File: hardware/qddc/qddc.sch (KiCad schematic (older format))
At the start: 37 parts, among them IC1 FST3253MTCX, IC2 OPA2350UA, J1 In_cos, J2 In_sin, J3 In_RF, J4 PWR, J5 Out_I, J6 Out_Q, T1 ETC4-1-2TR

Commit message: Start PCB for Quad DDC
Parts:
- C1, C10, C11, C12, C13, C2, C3, C4, C5, C6, C7, C8, C9: footprint (none) -> Capacitor_SMD:C_0805_2012Metric
- IC1: footprint SOP65P640X110-16N -> FST3253MTCX:SOP65P640X110-16N
- IC2: footprint SOIC127P600X175-8N -> OPA2350UA:SOIC127P600X175-8N
- J1, J2, J3, J5, J6: footprint (none) -> Connector_Coaxial:SMA_Amphenol_132289_EdgeMount
- J4: footprint (none) -> Connector_PinHeader_2.54mm:PinHeader_1x04_P2.54mm_Vertical
- L1: footprint (none) -> Inductor_SMD:L_1206_3216Metric
- R1, R10, R11, R12, R13, R14, R2, R3, R4, R5, R6, R7, R8, R9: footprint (none) -> Resistor_SMD:R_0805_2012Metric
- T1: footprint E_SERIES_1 -> ETC4-1-2TR:E_SERIES_1
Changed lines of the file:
@@
 F 0 "IC1" H 4550 2915 50  0000 C CNN
 F 1 "FST3253MTCX" H 4550 2824 50  0000 C CNN
-F 2 "SOP65P640X110-16N" H 4950 2750 50  0001 L CNN
+F 2 "FST3253MTCX:SOP65P640X110-16N" H 4950 2750 50  0001 L CNN
 F 3 "https://componentsearchengine.com/Datasheets/2/FST3253MTCX.pdf" H 4950 2650 50  0001 L CNN
 F 4 "IC, Fairchild, FST3253MTCX Fairchild Semiconductor FST3253MTCX, Multiplexer/Demultiplexer Dual 4:1 Multiplexer, 4  5.5 V, 16-Pin TSSOP" H 4950 2550 50  0001 L CNN "Description"
@@
 F 0 "T1" H 2625 3575 50  0000 C CNN
 F 1 "ETC4-1-2TR" H 2625 3484 50  0000 C CNN
-F 2 "E_SERIES_1" H 3400 3400 50  0001 L CNN
+F 2 "ETC4-1-2TR:E_SERIES_1" H 3400 3400 50  0001 L CNN
 F 3 "https://cdn.macom.com/datasheets/ETC4-1-2-TR.pdf" H 3400 3300 50  0001 L CNN
 F 4 "Audio Transformers / Signal Transformers 2-800MHz Imp. Ratio 1:4" H 3400 3200 50  0001 L CNN "Description"
@@
 F 0 "J3" H 1950 3532 50  0000 L CNN
 F 1 "In_RF" H 1950 3623 50  0000 L CNN
-F 2 "" H 1850 3650 50  0001 C CNN
+F 2 "Connector_Coaxial:SMA_Amphenol_132289_EdgeMount" H 1850 3650 50  0001 C CNN
 F 3 " ~" H 1850 3650 50  0001 C CNN
 	1    1850 3650
@@
 F 0 "R3" V 3093 3250 50  0000 C CNN
 F 1 "47" V 3184 3250 50  0000 C CNN
-F 2 "" V 3230 3250 50  0001 C CNN
+F 2 "Resistor_SMD:R_0805_2012Metric" V 3230 3250 50  0001 C CNN
 F 3 "~" H 3300 3250 50  0001 C CNN
 	1    3300 3250
@@
 F 0 "R4" V 3093 3650 50  0000 C CNN
 F 1 "47" V 3184 3650 50  0000 C CNN
-F 2 "" V 3230 3650 50  0001 C CNN
+F 2 "Resistor_SMD:R_0805_2012Metric" V 3230 3650 50  0001 C CNN
 F 3 "~" H 3300 3650 50  0001 C CNN
 	1    3300 3650
@@
 F 0 "R7" V 6243 2950 50  0000 C CNN
 F 1 "100" V 6334 2950 50  0000 C CNN
-F 2 "" V 6380 2950 50  0001 C CNN
+F 2 "Resistor_SMD:R_0805_2012Metric" V 6380 2950 50  0001 C CNN
 F 3 "~" H 6450 2950 50  0001 C CNN
 	1    6450 2950
@@
 F 0 "R8" V 6243 3250 50  0000 C CNN
 F 1 "100" V 6334 3250 50  0000 C CNN
-F 2 "" V 6380 3250 50  0001 C CNN
+F 2 "Resistor_SMD:R_0805_2012Metric" V 6380 3250 50  0001 C CNN
 F 3 "~" H 6450 3250 50  0001 C CNN
 	1    6450 3250
@@
 F 0 "R9" V 6243 3650 50  0000 C CNN
 F 1 "100" V 6334 3650 50  0000 C CNN
-F 2 "" V 6380 3650 50  0001 C CNN
+F 2 "Resistor_SMD:R_0805_2012Metric" V 6380 3650 50  0001 C CNN
 F 3 "~" H 6450 3650 50  0001 C CNN
 	1    6450 3650
@@
 F 0 "R10" V 6243 3950 50  0000 C CNN
 F 1 "100" V 6334 3950 50  0000 C CNN
-F 2 "" V 6380 3950 50  0001 C CNN
+F 2 "Resistor_SMD:R_0805_2012Metric" V 6380 3950 50  0001 C CNN
 F 3 "~" H 6450 3950 50  0001 C CNN
 	1    6450 3950
@@
 F 0 "C7" H 6315 2446 50  0000 L CNN
 F 1 "22nF" H 6315 2355 50  0000 L CNN
-F 2 "" H 6238 2250 50  0001 C CNN
+F 2 "Capacitor_SMD:C_0805_2012Metric" H 6238 2250 50  0001 C CNN
 F 3 "~" H 6200 2400 50  0001 C CNN
 	1    6200 2400
@@
 F 0 "C5" H 5915 2446 50  0000 L CNN
 F 1 "22nF" H 5915 2355 50  0000 L CNN
-F 2 "" H 5838 2250 50  0001 C CNN
+F 2 "Capacitor_SMD:C_0805_2012Metric" H 5838 2250 50  0001 C CNN
 F 3 "~" H 5800 2400 50  0001 C CNN
 	1    5800 2400
@@
 F 0 "C8" H 6315 4346 50  0000 L CNN
 F 1 "22nF" H 6315 4255 50  0000 L CNN
-F 2 "" H 6238 4150 50  0001 C CNN
+F 2 "Capacitor_SMD:C_0805_2012Metric" H 6238 4150 50  0001 C CNN
 F 3 "~" H 6200 4300 50  0001 C CNN
 	1    6200 4300
@@
 F 0 "C6" H 5915 4346 50  0000 L CNN
 F 1 "22nF" H 5915 4255 50  0000 L CNN
-F 2 "" H 5838 4150 50  0001 C CNN
+F 2 "Capacitor_SMD:C_0805_2012Metric" H 5838 4150 50  0001 C CNN
 F 3 "~" H 5800 4300 50  0001 C CNN
 	1    5800 4300
@@
 F 0 "J2" H 1949 2632 50  0000 L CNN
 F 1 "In_sin" H 1949 2723 50  0000 L CNN
-F 2 "" H 1850 2750 50  0001 C CNN
+F 2 "Connector_Coaxial:SMA_Amphenol_132289_EdgeMount" H 1850 2750 50  0001 C CNN
 F 3 " ~" H 1850 2750 50  0001 C CNN
 	1    1850 2750
@@
 F 0 "C9" H 6665 2446 50  0000 L CNN
 F 1 "390" H 6665 2355 50  0000 L CNN
-F 2 "" H 6588 2250 50  0001 C CNN
+F 2 "Capacitor_SMD:C_0805_2012Metric" H 6588 2250 50  0001 C CNN
 F 3 "~" H 6550 2400 50  0001 C CNN
 	1    6550 2400
@@
 F 0 "R11" H 6970 2446 50  0000 L CNN
 F 1 "2.2k" H 6970 2355 50  0000 L CNN
-F 2 "" V 6830 2400 50  0001 C CNN
+F 2 "Resistor_SMD:R_0805_2012Metric" V 6830 2400 50  0001 C CNN
 F 3 "~" H 6900 2400 50  0001 C CNN
 	1    6900 2400
@@
 F 0 "R12" V 7293 2150 50  0000 C CNN
 F 1 "100" V 7384 2150 50  0000 C CNN
-F 2 "" V 7430 2150 50  0001 C CNN
+F 2 "Resistor_SMD:R_0805_2012Metric" V 7430 2150 50  0001 C CNN
 F 3 "~" H 7500 2150 50  0001 C CNN
 	1    7500 2150
@@
 F 0 "R13" H 8870 2996 50  0000 L CNN
 F 1 "100" H 8870 2905 50  0000 L CNN
-F 2 "" V 8730 2950 50  0001 C CNN
+F 2 "Resistor_SMD:R_0805_2012Metric" V 8730 2950 50  0001 C CNN
 F 3 "~" H 8800 2950 50  0001 C CNN
 	1    8800 2950
@@
 F 0 "J6" H 9600 2675 50  0000 L CNN
 F 1 "Out_Q" H 9600 2584 50  0000 L CNN
-F 2 "" H 9500 2700 50  0001 C CNN
+F 2 "Connector_Coaxial:SMA_Amphenol_132289_EdgeMount" H 9500 2700 50  0001 C CNN
 F 3 " ~" H 9500 2700 50  0001 C CNN
 	1    9500 2700
@@
 F 0 "J5" H 9600 2125 50  0000 L CNN
 F 1 "Out_I" H 9600 2034 50  0000 L CNN
-F 2 "" H 9500 2150 50  0001 C CNN
+F 2 "Connector_Coaxial:SMA_Amphenol_132289_EdgeMount" H 9500 2150 50  0001 C CNN
 F 3 " ~" H 9500 2150 50  0001 C CNN
 	1    9500 2150
@@
 F 0 "R2" V 3093 2750 50  0000 C CNN
 F 1 "100" V 3184 2750 50  0000 C CNN
-F 2 "" V 3230 2750 50  0001 C CNN
+F 2 "Resistor_SMD:R_0805_2012Metric" V 3230 2750 50  0001 C CNN
 F 3 "~" H 3300 2750 50  0001 C CNN
 	1    3300 2750
@@
 F 0 "R1" V 3093 2150 50  0000 C CNN
 F 1 "100" V 3184 2150 50  0000 C CNN
-F 2 "" V 3230 2150 50  0001 C CNN
+F 2 "Resistor_SMD:R_0805_2012Metric" V 3230 2150 50  0001 C CNN
 F 3 "~" H 3300 2150 50  0001 C CNN
 	1    3300 2150
@@
 F 0 "R5" H 4020 4996 50  0000 L CNN
 F 1 "1k" H 4020 4905 50  0000 L CNN
-F 2 "" V 3880 4950 50  0001 C CNN
+F 2 "Resistor_SMD:R_0805_2012Metric" V 3880 4950 50  0001 C CNN
 F 3 "~" H 3950 4950 50  0001 C CNN
 	1    3950 4950
@@
 F 0 "R6" H 4020 5396 50  0000 L CNN
 F 1 "1k" H 4020 5305 50  0000 L CNN
-F 2 "" V 3880 5350 50  0001 C CNN
+F 2 "Resistor_SMD:R_0805_2012Metric" V 3880 5350 50  0001 C CNN
 F 3 "~" H 3950 5350 50  0001 C CNN
 	1    3950 5350
@@
 F 0 "C3" H 4465 5196 50  0000 L CNN
 F 1 "100nF" H 4465 5105 50  0000 L CNN
-F 2 "" H 4388 5000 50  0001 C CNN
+F 2 "Capacitor_SMD:C_0805_2012Metric" H 4388 5000 50  0001 C CNN
 F 3 "~" H 4350 5150 50  0001 C CNN
 	1    4350 5150
@@
 F 0 "C1" H 3115 5396 50  0000 L CNN
 F 1 "100nF" H 3115 5305 50  0000 L CNN
-F 2 "" H 3038 5200 50  0001 C CNN
+F 2 "Capacitor_SMD:C_0805_2012Metric" H 3038 5200 50  0001 C CNN
 F 3 "~" H 3000 5350 50  0001 C CNN
 	1    3000 5350
@@
 F 0 "C2" H 3618 5396 50  0000 L CNN
 F 1 "10nF" H 3618 5305 50  0000 L CNN
-F 2 "" H 3538 5200 50  0001 C CNN
+F 2 "Capacitor_SMD:C_0805_2012Metric" H 3538 5200 50  0001 C CNN
 F 3 "~" H 3500 5350 50  0001 C CNN
 	1    3500 5350
@@
 F 0 "L1" V 4840 4700 50  0000 C CNN
 F 1 "47uH" V 4749 4700 50  0000 C CNN
-F 2 "" H 4650 4700 50  0001 C CNN
+F 2 "Inductor_SMD:L_1206_3216Metric" H 4650 4700 50  0001 C CNN
 F 3 "~" H 4650 4700 50  0001 C CNN
 	1    4650 4700
@@
 F 0 "C4" H 5265 2446 50  0000 L CNN
 F 1 "100nF" H 5265 2355 50  0000 L CNN
-F 2 "" H 5188 2250 50  0001 C CNN
+F 2 "Capacitor_SMD:C_0805_2012Metric" H 5188 2250 50  0001 C CNN
 F 3 "~" H 5150 2400 50  0001 C CNN
 	1    5150 2400
@@
 F 0 "J1" H 1950 2032 50  0000 L CNN
 F 1 "In_cos" H 1950 2123 50  0000 L CNN
-F 2 "" H 1850 2150 50  0001 C CNN
+F 2 "Connector_Coaxial:SMA_Amphenol_132289_EdgeMount" H 1850 2150 50  0001 C CNN
 F 3 " ~" H 1850 2150 50  0001 C CNN
 	1    1850 2150
@@
 F 0 "C10" H 9315 3646 50  0000 L CNN
 F 1 "390" H 9315 3555 50  0000 L CNN
-F 2 "" H 9238 3450 50  0001 C CNN
+F 2 "Capacitor_SMD:C_0805_2012Metric" H 9238 3450 50  0001 C CNN
 F 3 "~" H 9200 3600 50  0001 C CNN
 	1    9200 3600
@@
 F 0 "IC2" H 7750 3415 50  0000 C CNN
 F 1 "OPA2350UA" H 7750 3324 50  0000 C CNN
-F 2 "SOIC127P600X175-8N" H 8200 3250 50  0001 L CNN
+F 2 "OPA2350UA:SOIC127P600X175-8N" H 8200 3250 50  0001 L CNN
 F 3 "http://www.ti.com/lit/ds/symlink/opa2350.pdf" H 8200 3150 50  0001 L CNN
 F 4 "High-Speed, Single-Supply, Rail-to-Rail Operational Amplifiers MicroAmplifier Series" H 8200 3050 50  0001 L CNN "Description"
@@
 F 0 "R14" H 8870 3646 50  0000 L CNN
 F 1 "2.2k" H 8870 3555 50  0000 L CNN
-F 2 "" V 8730 3600 50  0001 C CNN
+F 2 "Resistor_SMD:R_0805_2012Metric" V 8730 3600 50  0001 C CNN
 F 3 "~" H 8800 3600 50  0001 C CNN
 	1    8800 3600
@@
 F 0 "J4" H 8072 4624 50  0000 R CNN
 F 1 "PWR" H 8072 4533 50  0000 R CNN
-F 2 "" H 8100 4650 50  0001 C CNN
+F 2 "Connector_PinHeader_2.54mm:PinHeader_1x04_P2.54mm_Vertical" H 8100 4650 50  0001 C CNN
 F 3 "~" H 8100 4650 50  0001 C CNN
 	1    8100 4650
@@
 F 0 "C11" H 8465 2896 50  0000 L CNN
 F 1 "100nF" H 8465 2805 50  0000 L CNN
-F 2 "" H 8388 2700 50  0001 C CNN
+F 2 "Capacitor_SMD:C_0805_2012Metric" H 8388 2700 50  0001 C CNN
 F 3 "~" H 8350 2850 50  0001 C CNN
 	1    8350 2850
@@
 F 0 "C12" V 8798 2150 50  0000 C CNN
 F 1 "470nF" V 8889 2150 50  0000 C CNN
-F 2 "" H 9088 2000 50  0001 C CNN
+F 2 "Capacitor_SMD:C_0805_2012Metric" H 9088 2000 50  0001 C CNN
 F 3 "~" H 9050 2150 50  0001 C CNN
 	1    9050 2150
@@
 F 0 "C13" V 8798 2700 50  0000 C CNN
 F 1 "470nF" V 8889 2700 50  0000 C CNN
-F 2 "" H 9088 2550 50  0001 C CNN
+F 2 "Capacitor_SMD:C_0805_2012Metric" H 9088 2550 50  0001 C CNN
 F 3 "~" H 9050 2700 50  0001 C CNN
 	1    9050 2700
@@
 	5800 2250 5150 2250
 $Comp
-L power:GND #PWR?
+L power:GND #PWR0104
 U 1 1 6023AE13
 P 5800 2100
-F 0 "#PWR?" H 5800 1850 50  0001 C CNN
+F 0 "#PWR0104" H 5800 1850 50  0001 C CNN
 F 1 "GND" H 5805 1927 50  0000 C CNN
 F 2 "" H 5800 2100 50  0001 C CNN

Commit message: PCB for Quad DDC
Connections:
- net GND: now also J4.1 (Pin_1); no longer J4.4 (Pin_4)
- net PTT: now also J4.4 (Pin_4); no longer J4.1 (Pin_1)
- net at IC2.6 (-IN_B), R10.1, R14.2: now also C10.1; no longer C10.2
- net at IC2.7 (OUT_B), R13.2, R14.1: now also C10.2; no longer C10.1
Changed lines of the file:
@@
 L power:GND #PWR0114
 U 1 1 602C6C44
-P 7200 4850
-F 0 "#PWR0114" H 7200 4600 50  0001 C CNN
-F 1 "GND" V 7205 4722 50  0000 R CNN
-F 2 "" H 7200 4850 50  0001 C CNN
-F 3 "" H 7200 4850 50  0001 C CNN
-	1    7200 4850
+P 7200 4550
+F 0 "#PWR0114" H 7200 4300 50  0001 C CNN
+F 1 "GND" V 7205 4422 50  0000 R CNN
+F 2 "" H 7200 4550 50  0001 C CNN
+F 3 "" H 7200 4550 50  0001 C CNN
+	1    7200 4550
 	0    1    1    0
 $EndComp
@@
 $EndComp
 Wire Wire Line
-	7200 4750 7550 4750
-Wire Wire Line
 	3000 3450 3000 5150
 Connection ~ 3000 5150
@@
 U 1 1 601C8840
 P 9200 3600
-F 0 "C10" H 9315 3646 50  0000 L CNN
-F 1 "390" H 9315 3555 50  0000 L CNN
+F 0 "C10" H 8950 3650 50  0000 L CNN
+F 1 "390" H 8950 3550 50  0000 L CNN
 F 2 "Capacitor_SMD:C_0805_2012Metric" H 9238 3450 50  0001 C CNN
 F 3 "~" H 9200 3600 50  0001 C CNN
 	1    9200 3600
-	1    0    0    -1
+	-1   0    0    1
 $EndComp
 $Comp
@@
 U 1 1 601C7CA8
 P 8800 3600
-F 0 "R14" H 8870 3646 50  0000 L CNN
-F 1 "2.2k" H 8870 3555 50  0000 L CNN
+F 0 "R14" H 8850 3650 50  0000 L CNN
+F 1 "2.2k" H 8850 3550 50  0000 L CNN
 F 2 "Resistor_SMD:R_0805_2012Metric" V 8730 3600 50  0001 C CNN
 F 3 "~" H 8800 3600 50  0001 C CNN
@@
 	6900 3250 7150 3250
 Connection ~ 7150 2150
-$Comp
-L power:PWR_FLAG #FLG0101
-U 1 1 60403D64
-P 7550 4950
-F 0 "#FLG0101" H 7550 5025 50  0001 C CNN
-F 1 "PWR_FLAG" H 7550 5123 50  0000 C CNN
-F 2 "" H 7550 4950 50  0001 C CNN
-F 3 "~" H 7550 4950 50  0001 C CNN
-	1    7550 4950
-	-1   0    0    1
-$EndComp
-Wire Wire Line
-	7550 4750 7900 4750
 $Comp
 L power:VAA #PWR0116
@@
 $EndComp
 $Comp
-L power:PWR_FLAG #FLG0102
-U 1 1 6041AEE4
-P 7550 4550
-F 0 "#FLG0102" H 7550 4625 50  0001 C CNN
-F 1 "PWR_FLAG" H 7550 4723 50  0000 C CNN
-F 2 "" H 7550 4550 50  0001 C CNN
-F 3 "~" H 7550 4550 50  0001 C CNN
-	1    7550 4550
-	1    0    0    -1
-$EndComp
-Wire Wire Line
-	7550 4750 7550 4950
-Connection ~ 7550 4750
-Wire Wire Line
-	7200 4850 7300 4850
-Wire Wire Line
-	7200 4650 7550 4650
-Wire Wire Line
-	7550 4550 7550 4650
-Connection ~ 7550 4650
-Wire Wire Line
-	7550 4650 7900 4650
-$Comp
-L power:PWR_FLAG #FLG0103
-U 1 1 60452C9E
-P 7300 5100
-F 0 "#FLG0103" H 7300 5175 50  0001 C CNN
-F 1 "PWR_FLAG" H 7300 5273 50  0000 C CNN
-F 2 "" H 7300 5100 50  0001 C CNN
-F 3 "~" H 7300 5100 50  0001 C CNN
-	1    7300 5100
-	-1   0    0    1
-$EndComp
-Wire Wire Line
-	7300 5100 7300 4850
-Connection ~ 7300 4850
-Wire Wire Line
-	7300 4850 7900 4850
-$Comp
 L power:GND #PWR0120
 U 1 1 6046F96A
@@
 	-1   0    0    -1
 $EndComp
-Text GLabel 7900 4550 0    50   Input ~ 0
-PTT
 Wire Wire Line
 	8800 2800 8800 2700
@@
 Wire Wire Line
 	5800 2100 5800 2250
+Wire Wire Line
+	7200 4550 7900 4550
+Wire Wire Line
+	7200 4650 7900 4650
+Wire Wire Line
+	7200 4750 7900 4750
+Text GLabel 7900 4850 0    50   Input ~ 0
+PTT
+$Comp
+L power:GND #PWR0109
+U 1 1 601C8E8F
+P 6850 5200
+F 0 "#PWR0109" H 6850 4950 50  0001 C CNN
+F 1 "GND" H 6855 5027 50  0000 C CNN
+F 2 "" H 6850 5200 50  0001 C CNN
+F 3 "" H 6850 5200 50  0001 C CNN
+	1    6850 5200
+	1    0    0    -1
+$EndComp
+$Comp
+L power:VAA #PWR0110
+U 1 1 601C99BE
+P 7100 5200
+F 0 "#PWR0110" H 7100 5050 50  0001 C CNN
+F 1 "VAA" H 7115 5373 50  0000 C CNN
+F 2 "" H 7100 5200 50  0001 C CNN
+F 3 "" H 7100 5200 50  0001 C CNN
+	1    7100 5200
+	-1   0    0    1
+$EndComp
+$Comp
+L power:VCC #PWR0111
+U 1 1 601CA862
+P 7350 5200
+F 0 "#PWR0111" H 7350 5050 50  0001 C CNN
+F 1 "VCC" H 7365 5373 50  0000 C CNN
+F 2 "" H 7350 5200 50  0001 C CNN
+F 3 "" H 7350 5200 50  0001 C CNN
+	1    7350 5200
+	-1   0    0    1
+$EndComp
+$Comp
+L power:PWR_FLAG #FLG0101
+U 1 1 601CB67A
+P 6850 5200
+F 0 "#FLG0101" H 6850 5275 50  0001 C CNN
+F 1 "PWR_FLAG" H 6850 5373 50  0000 C CNN
+F 2 "" H 6850 5200 50  0001 C CNN
+F 3 "~" H 6850 5200 50  0001 C CNN
+	1    6850 5200
+	1    0    0    -1
+$EndComp
+$Comp
+L power:PWR_FLAG #FLG0102
+U 1 1 601CBF96
+P 7100 5200
+F 0 "#FLG0102" H 7100 5275 50  0001 C CNN
+F 1 "PWR_FLAG" H 7100 5373 50  0000 C CNN
+F 2 "" H 7100 5200 50  0001 C CNN
+F 3 "~" H 7100 5200 50  0001 C CNN
+	1    7100 5200
+	1    0    0    -1
+$EndComp
+$Comp
+L power:PWR_FLAG #FLG0103
+U 1 1 601CC85C
+P 7350 5200
+F 0 "#FLG0103" H 7350 5275 50  0001 C CNN
+F 1 "PWR_FLAG" H 7350 5373 50  0000 C CNN
+F 2 "" H 7350 5200 50  0001 C CNN
+F 3 "~" H 7350 5200 50  0001 C CNN
+	1    7350 5200
+	1    0    0    -1
+$EndComp
 $EndSCHEMATC

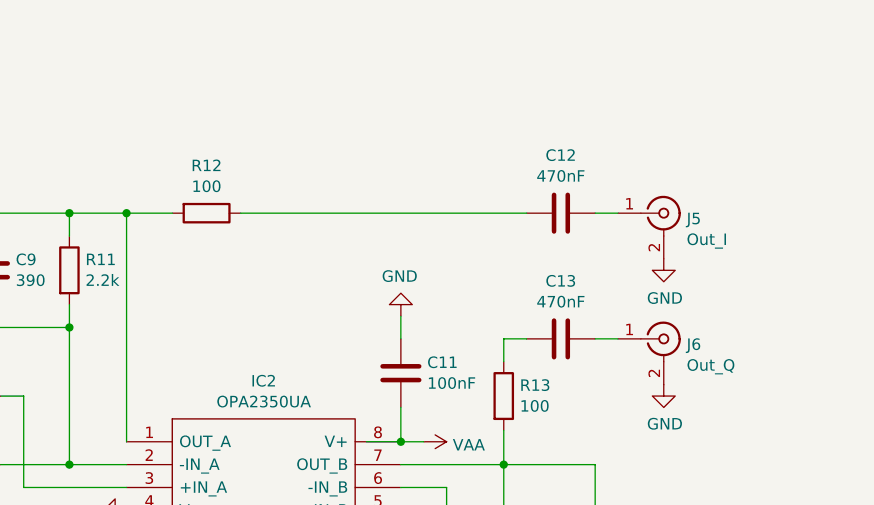
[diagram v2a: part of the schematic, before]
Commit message: Done PCB for Quad DDC
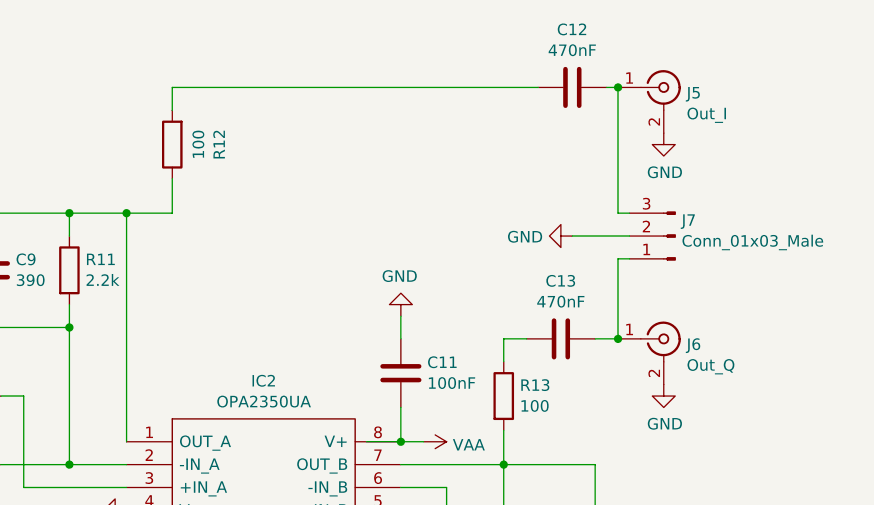
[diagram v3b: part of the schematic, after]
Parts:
- added J7: Conn_01x03_Male, Connector_PinHeader_2.54mm:PinHeader_1x03_P2.54mm_Vertical, symbol Connector:Conn_01x03_Male
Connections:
- net GND: now also J7.2 (Pin_2)
- net at C9.1, IC2.1 (OUT_A), R11.1: now also R12.1; no longer R12.2
- net at C12.1, J5.1 (In): now also J7.3 (Pin_3)
- net at C12.2: now also R12.2; no longer R12.1
- net at C13.1, J6.1 (In): now also J7.1 (Pin_1)
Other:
- moved on the sheet: C12, J5, R12
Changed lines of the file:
@@
 Sheet 1 1
 Title "Quad DDC"
-Date "2021-01-30"
+Date "2021-02-04"
 Rev ""
 Comp "R1CBU"
@@
 L Device:R R12
 U 1 1 601C4F4D
-P 7500 2150
-F 0 "R12" V 7293 2150 50  0000 C CNN
-F 1 "100" V 7384 2150 50  0000 C CNN
-F 2 "Resistor_SMD:R_0805_2012Metric" V 7430 2150 50  0001 C CNN
-F 3 "~" H 7500 2150 50  0001 C CNN
-	1    7500 2150
-	0    1    1    0
+P 7350 1850
+F 0 "R12" V 7143 1850 50  0000 C CNN
+F 1 "100" V 7234 1850 50  0000 C CNN
+F 2 "Resistor_SMD:R_0805_2012Metric" V 7280 1850 50  0001 C CNN
+F 3 "~" H 7350 1850 50  0001 C CNN
+	1    7350 1850
+	-1   0    0    1
 $EndComp
 Wire Wire Line
@@
 L Connector:Conn_Coaxial J5
 U 1 1 601E0053
-P 9500 2150
-F 0 "J5" H 9600 2125 50  0000 L CNN
-F 1 "Out_I" H 9600 2034 50  0000 L CNN
-F 2 "Connector_Coaxial:SMA_Amphenol_132289_EdgeMount" H 9500 2150 50  0001 C CNN
-F 3 " ~" H 9500 2150 50  0001 C CNN
-	1    9500 2150
+P 9500 1600
+F 0 "J5" H 9600 1575 50  0000 L CNN
+F 1 "Out_I" H 9600 1484 50  0000 L CNN
+F 2 "Connector_Coaxial:SMA_Amphenol_132289_EdgeMount" H 9500 1600 50  0001 C CNN
+F 3 " ~" H 9500 1600 50  0001 C CNN
+	1    9500 1600
 	1    0    0    -1
 $EndComp
@@
 L power:GND #PWR0105
 U 1 1 601E9B5C
-P 9500 2350
-F 0 "#PWR0105" H 9500 2100 50  0001 C CNN
-F 1 "GND" H 9505 2177 50  0000 C CNN
-F 2 "" H 9500 2350 50  0001 C CNN
-F 3 "" H 9500 2350 50  0001 C CNN
-	1    9500 2350
+P 9500 1800
+F 0 "#PWR0105" H 9500 1550 50  0001 C CNN
+F 1 "GND" H 9505 1627 50  0000 C CNN
+F 2 "" H 9500 1800 50  0001 C CNN
+F 3 "" H 9500 1800 50  0001 C CNN
+	1    9500 1800
 	1    0    0    -1
 $EndComp
@@
 L Device:C C12
 U 1 1 6018E3D3
-P 9050 2150
-F 0 "C12" V 8798 2150 50  0000 C CNN
-F 1 "470nF" V 8889 2150 50  0000 C CNN
-F 2 "Capacitor_SMD:C_0805_2012Metric" H 9088 2000 50  0001 C CNN
-F 3 "~" H 9050 2150 50  0001 C CNN
-	1    9050 2150
+P 9100 1600
+F 0 "C12" V 8848 1600 50  0000 C CNN
+F 1 "470nF" V 8939 1600 50  0000 C CNN
+F 2 "Capacitor_SMD:C_0805_2012Metric" H 9138 1450 50  0001 C CNN
+F 3 "~" H 9100 1600 50  0001 C CNN
+	1    9100 1600
 	0    1    1    0
 $EndComp
@@
 $EndComp
 Wire Wire Line
-	7650 2150 8900 2150
-Wire Wire Line
-	9200 2150 9300 2150
+	9250 1600 9300 1600
 Wire Wire Line
 	8800 2700 8900 2700
@@
 	1    0    0    -1
 $EndComp
+Wire Wire Line
+	9300 1600 9300 2150
+Wire Wire Line
+	9300 2150 9350 2150
+Connection ~ 9300 1600
+Wire Wire Line
+	9350 2350 9300 2350
+Wire Wire Line
+	9300 2350 9300 2700
+Connection ~ 9300 2700
+$Comp
+L power:GND #PWR0112
+U 1 1 601FECFD
+P 9100 2250
+F 0 "#PWR0112" H 9100 2000 50  0001 C CNN
+F 1 "GND" V 9105 2122 50  0000 R CNN
+F 2 "" H 9100 2250 50  0001 C CNN
+F 3 "" H 9100 2250 50  0001 C CNN
+	1    9100 2250
+	0    1    1    0
+$EndComp
+Wire Wire Line
+	9100 2250 9350 2250
+Wire Wire Line
+	7350 2150 7350 2000
+Wire Wire Line
+	7350 1700 7350 1600
+Wire Wire Line
+	7350 1600 8950 1600
+$Comp
+L Connector:Conn_01x03_Male J7
+U 1 1 601CEB5E
+P 9550 2250
+F 0 "J7" H 9522 2182 50  0000 R CNN
+F 1 "Conn_01x03_Male" H 9522 2273 50  0000 R CNN
+F 2 "Connector_PinHeader_2.54mm:PinHeader_1x03_P2.54mm_Vertical" H 9550 2250 50  0001 C CNN
+F 3 "~" H 9550 2250 50  0001 C CNN
+	1    9550 2250
+	-1   0    0    1
+$EndComp
 $EndSCHEMATC
